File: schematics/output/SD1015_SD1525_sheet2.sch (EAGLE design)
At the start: 263 parts, among them J1 CONN, J2 CONN, J3 CONN, J4 CONN, J5 CONN, Q1 JFET, Q11 NPN, Q12 NPN, Q14 NPN, Q2 NPN, Q5 PNP, Q6 NMOS, Q7 NMOS, Q9 NPN, T1 XFMR, T2 XFMR, T3 XFMR, T4 XFMR, U1A OPAMP | U1 section, pins 1/2/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, U1B OPAMP | U1 section, pins 4/5/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, U2A OPAMP, U2B OPAMP | U2 section - A.V. AMP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, U2C OPAMP, U3 COMP, U4A NPN, U4B NPN, U4C NPN, U4D NPN, U5 IC, U6 IC, U7A IC, U7B IC, U7C IC, U7D IC, U8A OPAMP, U8B OPAMP, U9A OPAMP, U9B OPAMP | U9 section - ECC

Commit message: Fix C8 transcription: the -15 V rail was shorted to ground
C8 was transcribed with its plates the other way round in S1_input than in
S4_comp. The merge is union-find over shared pins, so the two readings tied
N15 and GND into one node. The -15 V rail did not exist in the output: all 16
of its pins (U1B.4, U8B.4, U9A.4, J1.12, J4.3, D44.1, and the R118/R119 +/-15 V
adjust divider) were reported as ground, and GND was 84 pins because it had
swallowed a supply.

S4_comp is the correct reading. C8 is drawn with its "+" on the grounded plate
-- right for a decoupler on a negative rail, and pin 1 is the "+" plate.
S1_input corrected to match. GND is now 68 pins, N15 has 16, and the 627 pin
connections are unchanged: nothing gained or lost, 16 pins simply stop being
ground.

I checked whether this was systemic. 14 pins are declared under two different
net names; 13 are benign aliases -- the same node named differently in two
sections, which is what the stitch marker exists for. C8 was the only genuine
contradiction, and the only one merging two distinct rails.

build_nets now raises ShortedRailsError if any two GLOBAL_ORDER names merge,
because the failure mode is silent -- the smaller rail simply disappears into
the larger. Test covers both the real design and a synthetic swap.

Netlist fixture and the net-count assertion regenerated: 165 -> 166 nets.

Co-Authored-By: Claude Opus 5 <noreply@anthropic.com>
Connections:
- new net N15: C42.2, C8.2, D44.1, J1.12, J4.3, R118.2, R118.3, R119.2, R119.3, R20.2, R38.2, R79.1, R87.2, U1B.4, U8B.4, U9A.4
- net GND: no longer C42.2, C8.2, D44.1, J1.12, J4.3, R118.2, R118.3, R119.2, R119.3, R20.2, R38.2, R79.1, R87.2, U1B.4, U8B.4, U9A.4

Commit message: Split into nine sheets with frames, and draw supplies as rail symbols
Two changes that together take the biggest bite out of the readability
complaint, neither of which needs a router.

Nine A3 sheets, one per functional block, replacing the single 475 x 1120 mm
page. Section sizes are 16-43 parts, so each fits comfortably. Every sheet
gets a <frame>: the document already set xreflabel="%F%N/%S.%C%R", but with no
frame there were no column/row references, so all 627 cross-reference labels
pointed at nothing. Now they resolve.

Supply and ground pins get a rail symbol instead of a label. SUPPLY_* devicesets
use direction="sup" so Fusion's ERC treats them as rails, and length="point" so
the instance sits exactly on the wire end with no offset arithmetic. That is
139 labels gone -- 68 GND, 36 P15, 16 N15, and the BUSCOM/CHASSIS/P100 pins.
Labels on the sheet drop from 627 to 488; the rest come off in the routing
phase.

Rail symbols are a drawing decoration, not transcribed design: they are created
by the router, never enter Design.parts or Design.nets, and validate.py counts
them separately. So netlist.csv and the 263/166/627 totals are untouched, and
test_regression.py passes unmodified -- the point of the seam added last commit.

R35B moves off the one-part MISC sheet to sit beside R31 in the compensation
block, via a SHEET_OF override.

validate.py now walks all sheets, tolerates segments with several wires and
pinrefs (the router will need that next), checks a part is drawn on the sheet
its net references it from, and checks each net reaches two real pins counting
across sheets.

--placement grid still regenerates the old single sheet byte-identically, kept
as the comparison baseline.

Fixed a wrong test invariant while here: placement uniqueness was asserted
globally, but two parts on different sheets may share a coordinate. It is a
per-sheet property.

Co-Authored-By: Claude Opus 5 <noreply@anthropic.com>
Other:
- note removed: "extra -- MISC"

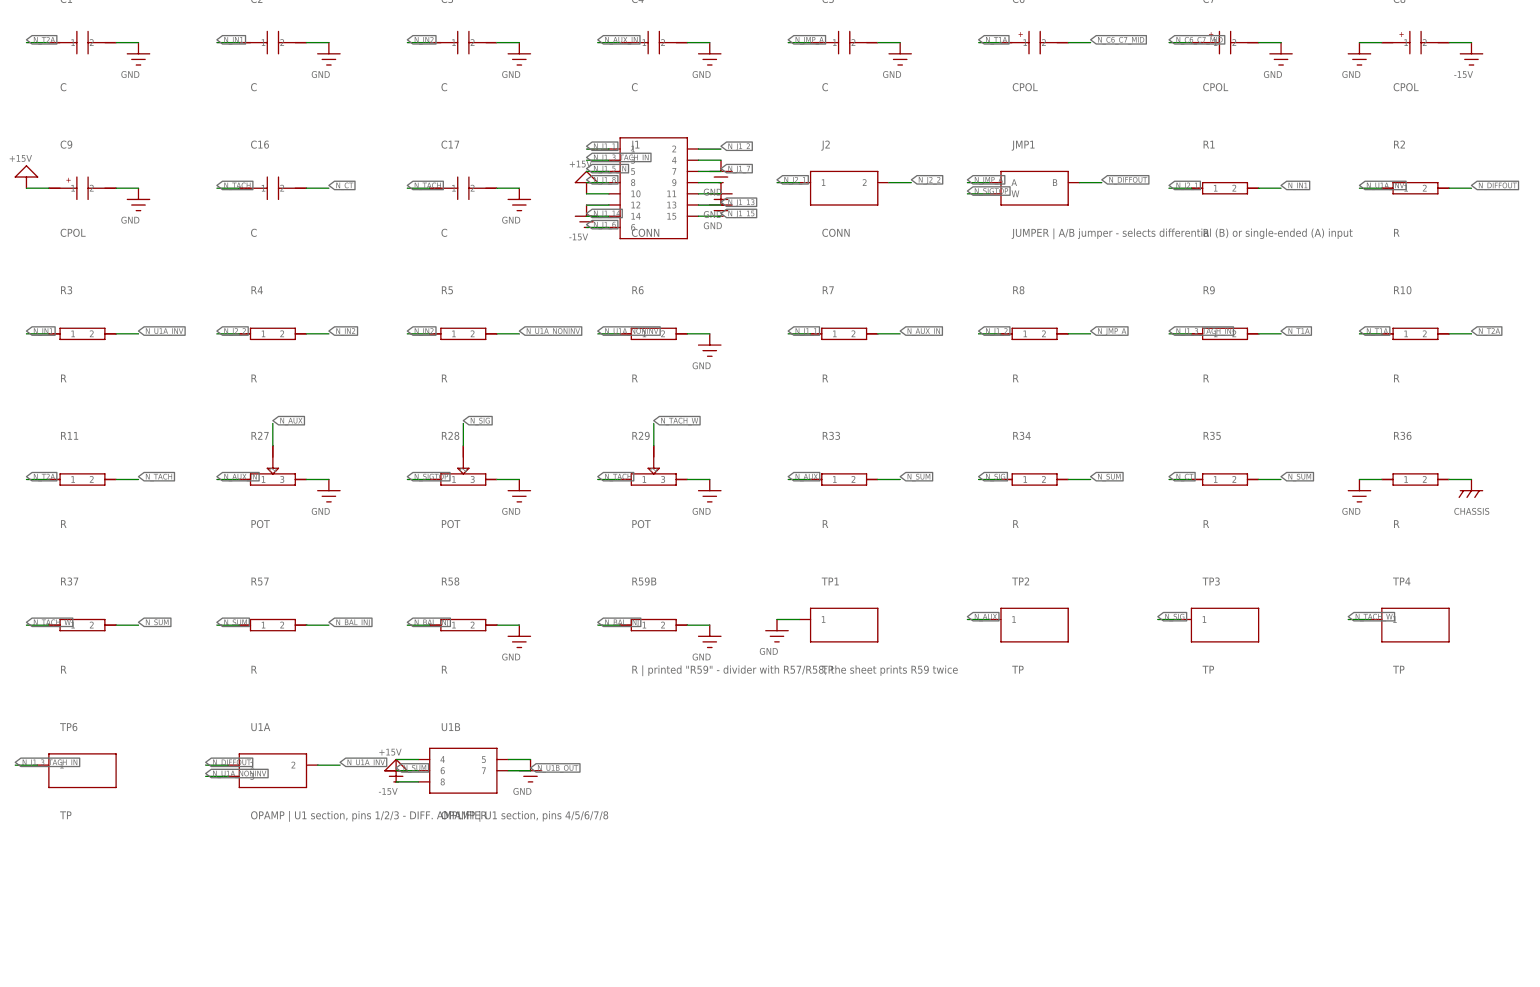
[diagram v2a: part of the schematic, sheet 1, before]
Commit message: Draw parts from pin roles, and give them real device symbols
Roles were positional: a part came out right only if its pins happened to be
transcribed in canonical order, and mostly they were not. U1A's output was
drawn on the left. U4A's collector sat in the base slot. Q7's grounded source
occupied the gate position. Seven of thirteen transistors were mis-slotted, and
PNP, NMOS and JFET all reused the NPN body with no arrow, gate bar or channel.
The netlist was right the whole time; the picture was not.

sections.py gains a ROLES table keyed by refdes, alongside the existing NOTES.
A pin already named B/C/E or G/D/S supplies its own role, which leaves sixteen
entries: ten amplifier sections, the four U4 array transistors, and Q6/Q7 whose
gate the drawing labels "E". Resolution is table, then pin name, then nothing --
there is no positional fallback, so an unresolvable part warns instead of being
drawn wrong. Roles came from the net names, which are self-documenting
(N_U4A_BASE, N_Q7_GATE, N_U3_OUT), cross-checked against each IC's pinout: the
base is the middle pin of every U4 section, and U1/U8/U9 read as an 8-pin dual.

Real symbols follow: amplifier triangles with inputs left and output right and
the rails drawn when known, bipolars with an emitter arrow that reverses for
PNP, MOSFETs with an insulated gate and a three-segment channel, JFETs with a
gate arrow, connectors as pin strips, test points as circles. Generic ICs run
their pins down one side in order instead of alternating by index parity, which
is what made U6 unreadable. Pins now carry real direction attributes, so Fusion
stops seeing the sheet as floating passives.

Symbol signatures include the role map, so two parts with the same pin names but
different roles can no longer collapse onto one symbol.

>VALUE no longer repeats the part kind -- it read a literal "R" under all 111
resistors. The kind moves to the deviceset description.

Sheet row pitch grows to 38.1 mm because real symbols are bigger than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
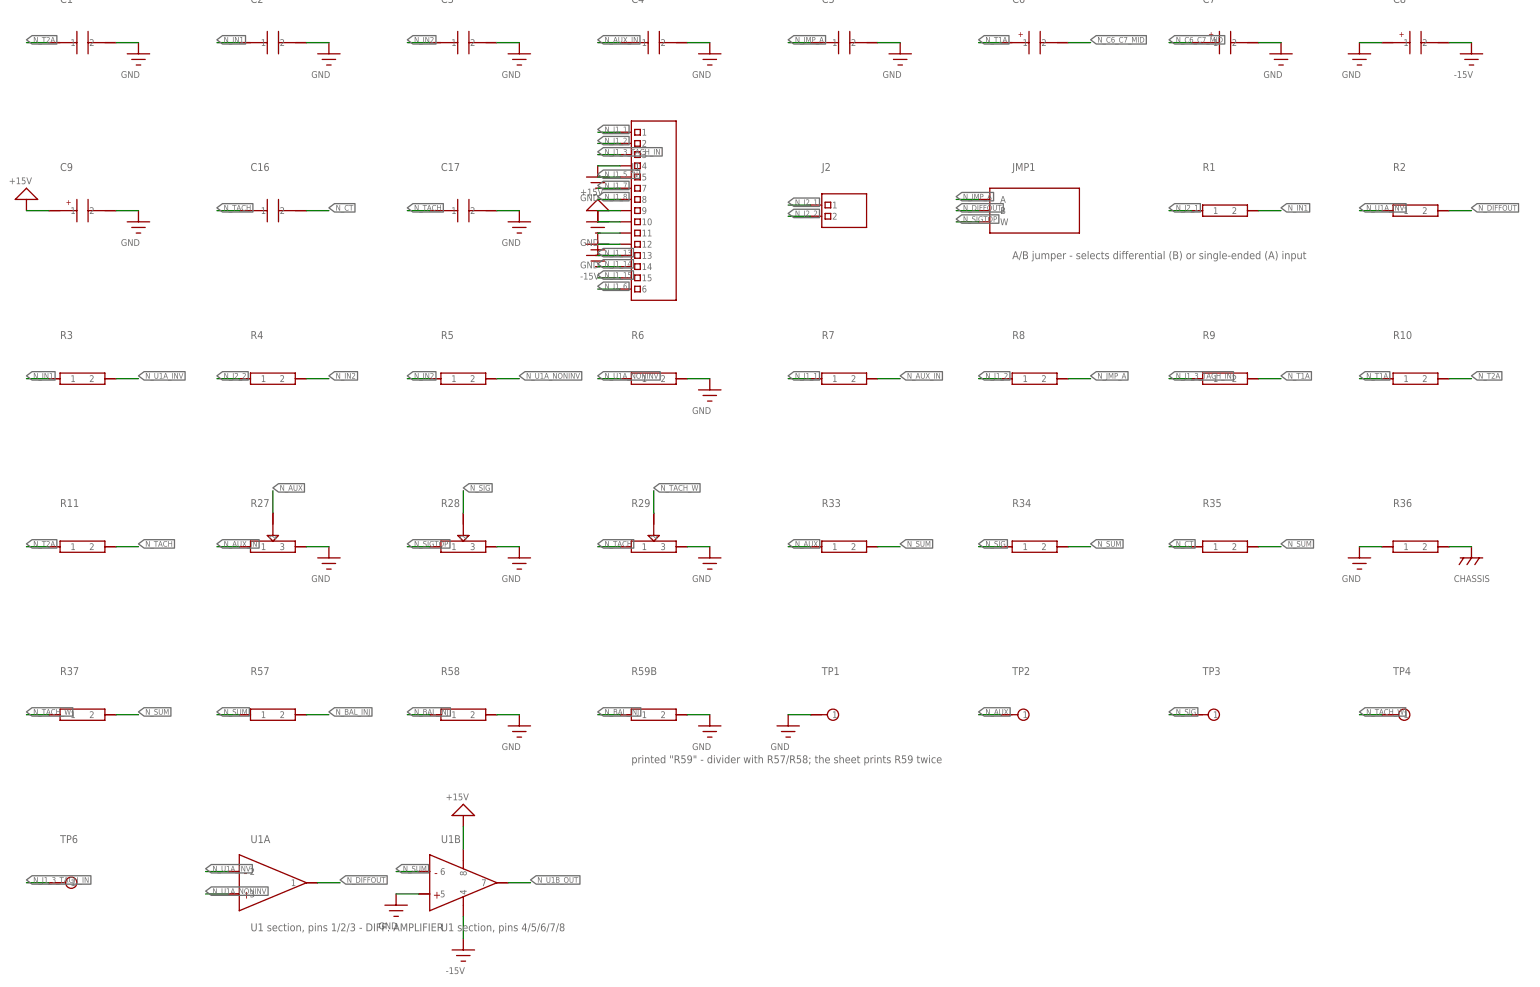
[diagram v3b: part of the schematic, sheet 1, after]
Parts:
- C1, C10, C11, C12, C16, C17, C18, C2, C20, C21, C22, C23, C27, C3, C30, C31, C36, C37, C38, C39, C4, C40, C41, C43, C44, C5, C52, C53, C55: value C -> (none)
- C42, C50, C51, C56, C6, C61, C7, C8, C9: value CPOL -> (none)
- CLOCK, DRIVER1, DRIVER2, LOCKOUT, PWM, RMSTIMER, SURGE_DETECTOR, TEMPSENSOR: value BLOCK -> (none)
- D1, D12, D13, D14, D15, D16, D17, D18, D19, D2, D24, D25, D3, D36, D37, D38, D39, D40, D41, D42, D43, D46, D47, D48, D49, D5, D50, D51, D52, D53, D6, D7, D8: value D -> (none)
- D10, D11, D12A, D44, D9: value ZENER -> (none)
- D78A, D78B, D78C, D78D: value D | one leg of the D78 bridge -> one leg of the D78 bridge
- FGF: value BLOCK | fuse, ground-fault detection (no refdes on drawing) -> fuse, ground-fault detection (no refdes on drawing)
- J1, J2, J3, J4, J5: value CONN -> (none)
- JMP1: value JUMPER | A/B jumper - selects differential (B) or single-ended (A) input -> A/B jumper - selects differential (B) or single-ended (A) input
- LED1, LED2, LED3, LED4: value LED -> (none)
- Q1: value JFET -> (none)
- Q11, Q12, Q14, Q2, Q9, U4A, U4B, U4C, U4D: value NPN -> (none)
- Q5: value PNP -> (none)
- Q6, Q7: value NMOS -> (none)
- R1, R10, R100, R102, R103, R104, R11, R113, R114, R115, R116, R117, R120, R121, R122, R123, R124, R125, R126, R12A, R13, R130, R131, R132, R133, R134, R135, R136, R14, R142, R144, R147, R149, R15, R150, R153, R154, R155, R156, R16, R19, R2, R20, R21, R3, R33, R34, R35, R36, R37, R38, R39, R4, R40, R41, R42, R43, R45, R46, R47, R48, R49, R5, R50, R51, R52, R53, R54, R56, R57, R58, R59, R6, R60, R64A, R64B, R65, R66, R67, R68, R69, R7, R73, R76, R78A, R78B, R79, R8, R80A, R80B, R81, R82, R83, R84, R85, R86, R87, R88, R89, R9, R90, R91, R94, R95, R99: value R -> (none)
- R118, R119, R12B, R151, R27, R28, R29, R30, R31, R32, R44: value POT -> (none)
- R137: value R | printed "R137" (not R157) - +15 V decoupling to the driver centre tap -> printed "R137" (not R157) - +15 V decoupling to the driver centre tap
- R157: value R | series element in the J5 pin 10/11 motor lead -> series element in the J5 pin 10/11 motor lead
- R35B: value R | printed "R35" - current-limit pot return; the sheet prints R35 twice -> printed "R35" - current-limit pot return; the sheet prints R35 twice
- R59B: value R | printed "R59" - divider with R57/R58; the sheet prints R59 twice -> printed "R59" - divider with R57/R58; the sheet prints R59 twice
- R60B: value R | printed "R60" - balance-pot series element; the sheet prints R60 twice -> printed "R60" - balance-pot series element; the sheet prints R60 twice
- RGF: value R | 10 ohm 12 W chassis resistor, ground-fault detection (no refdes on drawing) -> 10 ohm 12 W chassis resistor, ground-fault detection (no refdes on drawing)
- S1: value JUMPER | RESET BUTTON (momentary) -> RESET BUTTON (momentary)
- T1, T2, T3, T4: value XFMR -> (none)
- TP1, TP2, TP3, TP4, TP5, TP6, TP7, TP8: value TP -> (none)
- U1A: value OPAMP | U1 section, pins 1/2/3 - DIFF. AMPLIFIER -> U1 section, pins 1/2/3 - DIFF. AMPLIFIER
- U1B: value OPAMP | U1 section, pins 4/5/6/7/8 -> U1 section, pins 4/5/6/7/8
- U2A, U2C, U8A, U8B, U9A: value OPAMP -> (none)
- U2B: value OPAMP | U2 section - A.V. AMPLIFIER -> U2 section - A.V. AMPLIFIER
- U3: value COMP -> (none)
- U5, U6, U7A, U7B, U7C, U7D: value IC -> (none)
- U9B: value OPAMP | U9 section - ECC -> U9 section - ECC
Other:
- moved on the sheet: C16, C17, C9, D12A, D13, D14, D19, D25, D40, D41, D42, D43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
